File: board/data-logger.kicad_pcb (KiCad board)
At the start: 4 copper layers, 105 x 100 mm, 220 parts, among them P401 CONN_01X02, P402 CONN_01X04, P403 CONN_01X04, P501 CONN_02X03, P502 CONN_02X06, P503 MICROSD, P504 USB_B, P601 CONN_02X08, P602 CONN_02X08, P603 CONN_02X08, P604 CONN_02X08, Q401 IRLML6401, Q402 Q_NMOS_GSD, Q501 IRLML6401, U201 10M08DCF256, U202 AS4C8M16SA-7TCN, U203 AS4C8M16SA-7TCN, U302 SAM3U1EB-AU, U401 AP2138N-2.5TRG1, U402 LM4120, U403 BQ24161RGE, U404 TPS62097, U405 TPS62097, U406 AP2138N-2.5TRG1, U407 TPS63001, U501 LSF0204, U502 LSF0204, U601 MCP6002, X501 CONN_DEBUG_MCNET, X502 IQXO/7X, Y501 32.768 kHz, Y502 12.000MHz

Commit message: Save last pcb layout work
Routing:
- net Net-(C441-Pad1): track 0.71 -> 5.52 mm, vias 1 -> 2
- net /InterConnect/FPGA_CRC_ERROR: track 4.54 -> 8.15 mm, vias 0 -> 1
- net /InterConnect/SMC_D3: track 0.00 -> 3.61 mm, vias 0 -> 1
- net /InterConnect/SMC_D2: track 0.00 -> 3.61 mm, vias 0 -> 1
- net /InterConnect/SMC_D10: track 0.00 -> 3.56 mm, vias 0 -> 1
- net /InterConnect/SMC_NWAIT: track 0.00 -> 2.61 mm
- net /InterConnect/SMC_D11: track 0.00 -> 2.61 mm
- net /InterConnect/SMC_A14: track 0.00 -> 2.61 mm
- net /InterConnect/SMC_A12: track 0.00 -> 2.61 mm
- net /InterConnect/SMC_A17: track 0.00 -> 1.40 mm
- net /InterConnect/SMC_A16: track 0.00 -> 1.40 mm
- net /InterConnect/SMC_A15: track 0.00 -> 1.40 mm
- net /InterConnect/SMC_A13: track 0.00 -> 1.35 mm
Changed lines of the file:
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@@
   (general
     (links 900)
-    (no_connects 480)
-    (area 17.424999 33.424999 122.575001 133.575001)
+    (no_connects 464)
+    (area 13.174999 10.775 129.295001 149.100001)
     (thickness 1.6)
     (drawings 12)
-    (tracks 1926)
+    (tracks 1955)
     (zones 0)
     (modules 220)
@@
   )
   (setup
-    (last_trace_width 0.2)
+    (last_trace_width 0.15)
     (user_trace_width 0.15)
     (user_trace_width 0.2)
@@
   (segment (start 41.135998 108.5) (end 42.035998 107.6) (width 0.2) (layer F.Cu) (net 137))
   (segment (start 42.035998 107.6) (end 42.95 107.6) (width 0.2) (layer F.Cu) (net 137))
+  (segment (start 71.35 84.5) (end 68.45 84.5) (width 0.15) (layer B.Cu) (net 138))
+  (segment (start 71.85 84) (end 71.35 84.5) (width 0.15) (layer F.Cu) (net 138))
+  (via (at 71.35 84.5) (size 0.5) (drill 0.2) (layers F.Cu B.Cu) (net 138))
   (segment (start 42.95 105.6) (end 41.975 105.6) (width 0.2) (layer F.Cu) (net 138))
   (segment (start 41.975 105.6) (end 40.675 106.9) (width 0.2) (layer F.Cu) (net 138))
@@
   (segment (start 89.1 107.1) (end 89.1 106.225) (width 0.15) (layer F.Cu) (net 163))
   (segment (start 89.1 106.225) (end 88.475 105.6) (width 0.15) (layer F.Cu) (net 163))
+  (segment (start 69.85 87) (end 68.45 87) (width 0.15) (layer F.Cu) (net 166))
+  (segment (start 70.35 87.5) (end 68.45 87.5) (width 0.15) (layer F.Cu) (net 167))
+  (segment (start 70.85 87) (end 70.35 87.5) (width 0.15) (layer F.Cu) (net 167))
+  (segment (start 71.35 87.5) (end 68.5 87.5) (width 0.15) (layer B.Cu) (net 168))
+  (segment (start 71.85 87) (end 71.35 87.5) (width 0.15) (layer F.Cu) (net 168))
+  (via (at 71.35 87.5) (size 0.5) (drill 0.2) (layers F.Cu B.Cu) (net 168))
   (segment (start 42.95 110.6) (end 40.9 110.6) (width 0.2) (layer F.Cu) (net 172))
+  (segment (start 69.85 86) (end 68.45 86) (width 0.15) (layer F.Cu) (net 173))
+  (segment (start 70.35 86.5) (end 68.45 86.5) (width 0.15) (layer F.Cu) (net 174))
+  (segment (start 70.600001 86.249999) (end 70.35 86.5) (width 0.15) (layer F.Cu) (net 174))
+  (segment (start 70.85 86) (end 70.600001 86.249999) (width 0.15) (layer F.Cu) (net 174))
+  (segment (start 71.35 86.5) (end 68.45 86.5) (width 0.15) (layer B.Cu) (net 175))
+  (segment (start 71.85 86) (end 71.35 86.5) (width 0.15) (layer F.Cu) (net 175))
+  (via (at 71.35 86.5) (size 0.5) (drill 0.2) (layers F.Cu B.Cu) (net 175))
+  (segment (start 69.85 85) (end 68.45 85) (width 0.15) (layer F.Cu) (net 180))
+  (segment (start 70.35 85.5) (end 68.45 85.5) (width 0.15) (layer F.Cu) (net 181))
+  (segment (start 70.85 85) (end 70.35 85.5) (width 0.15) (layer F.Cu) (net 181))
+  (segment (start 71.35 85.5) (end 68.45 85.5) (width 0.15) (layer B.Cu) (net 182))
+  (via (at 71.35 85.5) (size 0.5) (drill 0.2) (layers F.Cu B.Cu) (net 182))
+  (segment (start 71.85 85) (end 71.35 85.5) (width 0.15) (layer F.Cu) (net 182))
+  (segment (start 69.85 84) (end 68.5 84) (width 0.15) (layer F.Cu) (net 186))
+  (segment (start 70.35 84.5) (end 68.45 84.5) (width 0.15) (layer F.Cu) (net 187))
+  (segment (start 70.85 84) (end 70.35 84.5) (width 0.15) (layer F.Cu) (net 187))
   (segment (start 71.385 36.6) (end 80.95 36.6) (width 0.3) (layer F.Cu) (net 212))
   (segment (start 92.25 36.6) (end 95.285 36.6) (width 0.3) (layer F.Cu) (net 212))
@@
   (segment (start 33.235 45.2) (end 32.15 45.2) (width 0.3) (layer F.Cu) (net 263))
   (segment (start 32.15 45.2) (end 31.7 44.75) (width 0.3) (layer F.Cu) (net 263))
+  (segment (start 71.85 85) (end 68.45 85) (width 0.15) (layer B.Cu) (net 265))
+  (segment (start 72.35 84.5) (end 71.85 85) (width 0.15) (layer B.Cu) (net 265))
+  (segment (start 72.85 84) (end 72.35 84.5) (width 0.15) (layer F.Cu) (net 265))
+  (via (at 72.35 84.5) (size 0.5) (drill 0.2) (layers F.Cu B.Cu) (net 265))
   (via (at 80.35 77.5) (size 0.5) (drill 0.2) (layers F.Cu B.Cu) (net 265))
   (segment (start 80.85 77) (end 80.35 77.5) (width 0.3) (layer F.Cu) (net 265))

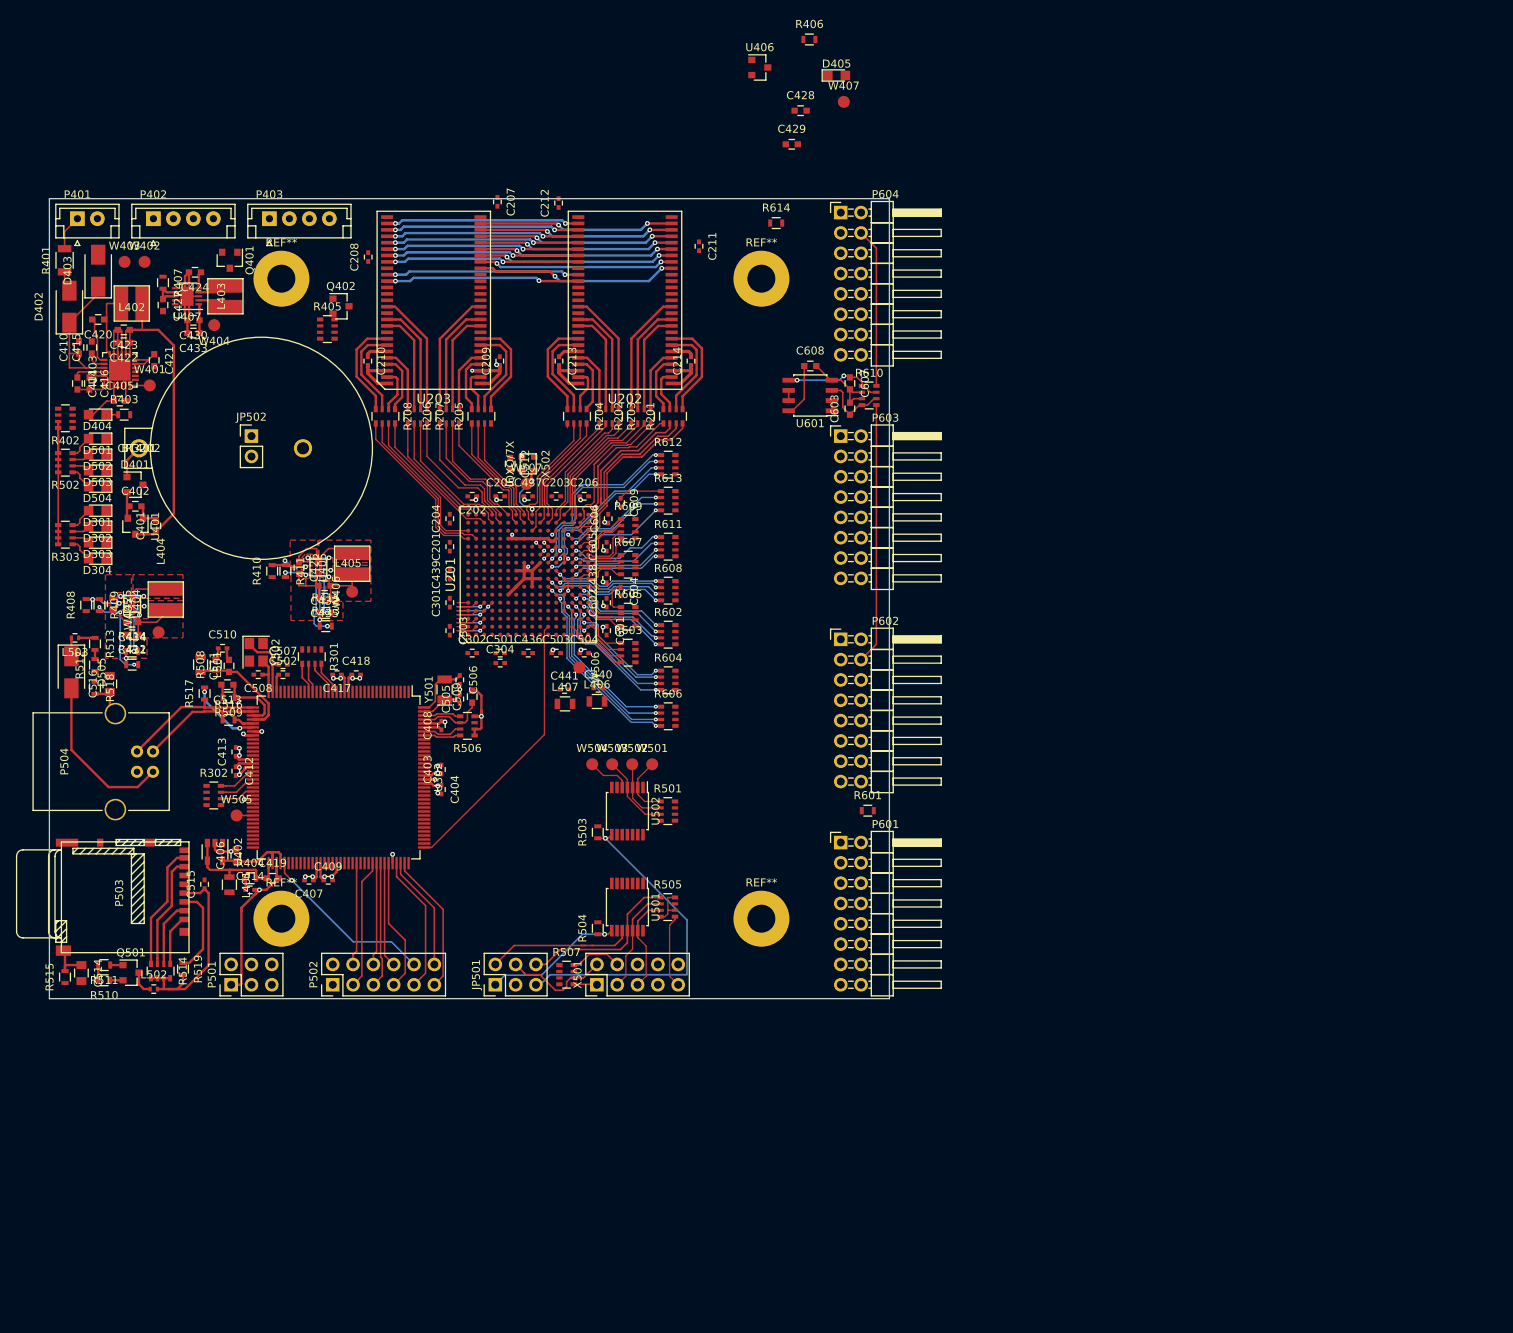
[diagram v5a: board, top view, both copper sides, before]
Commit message: Some initial DDR3 Ram routing
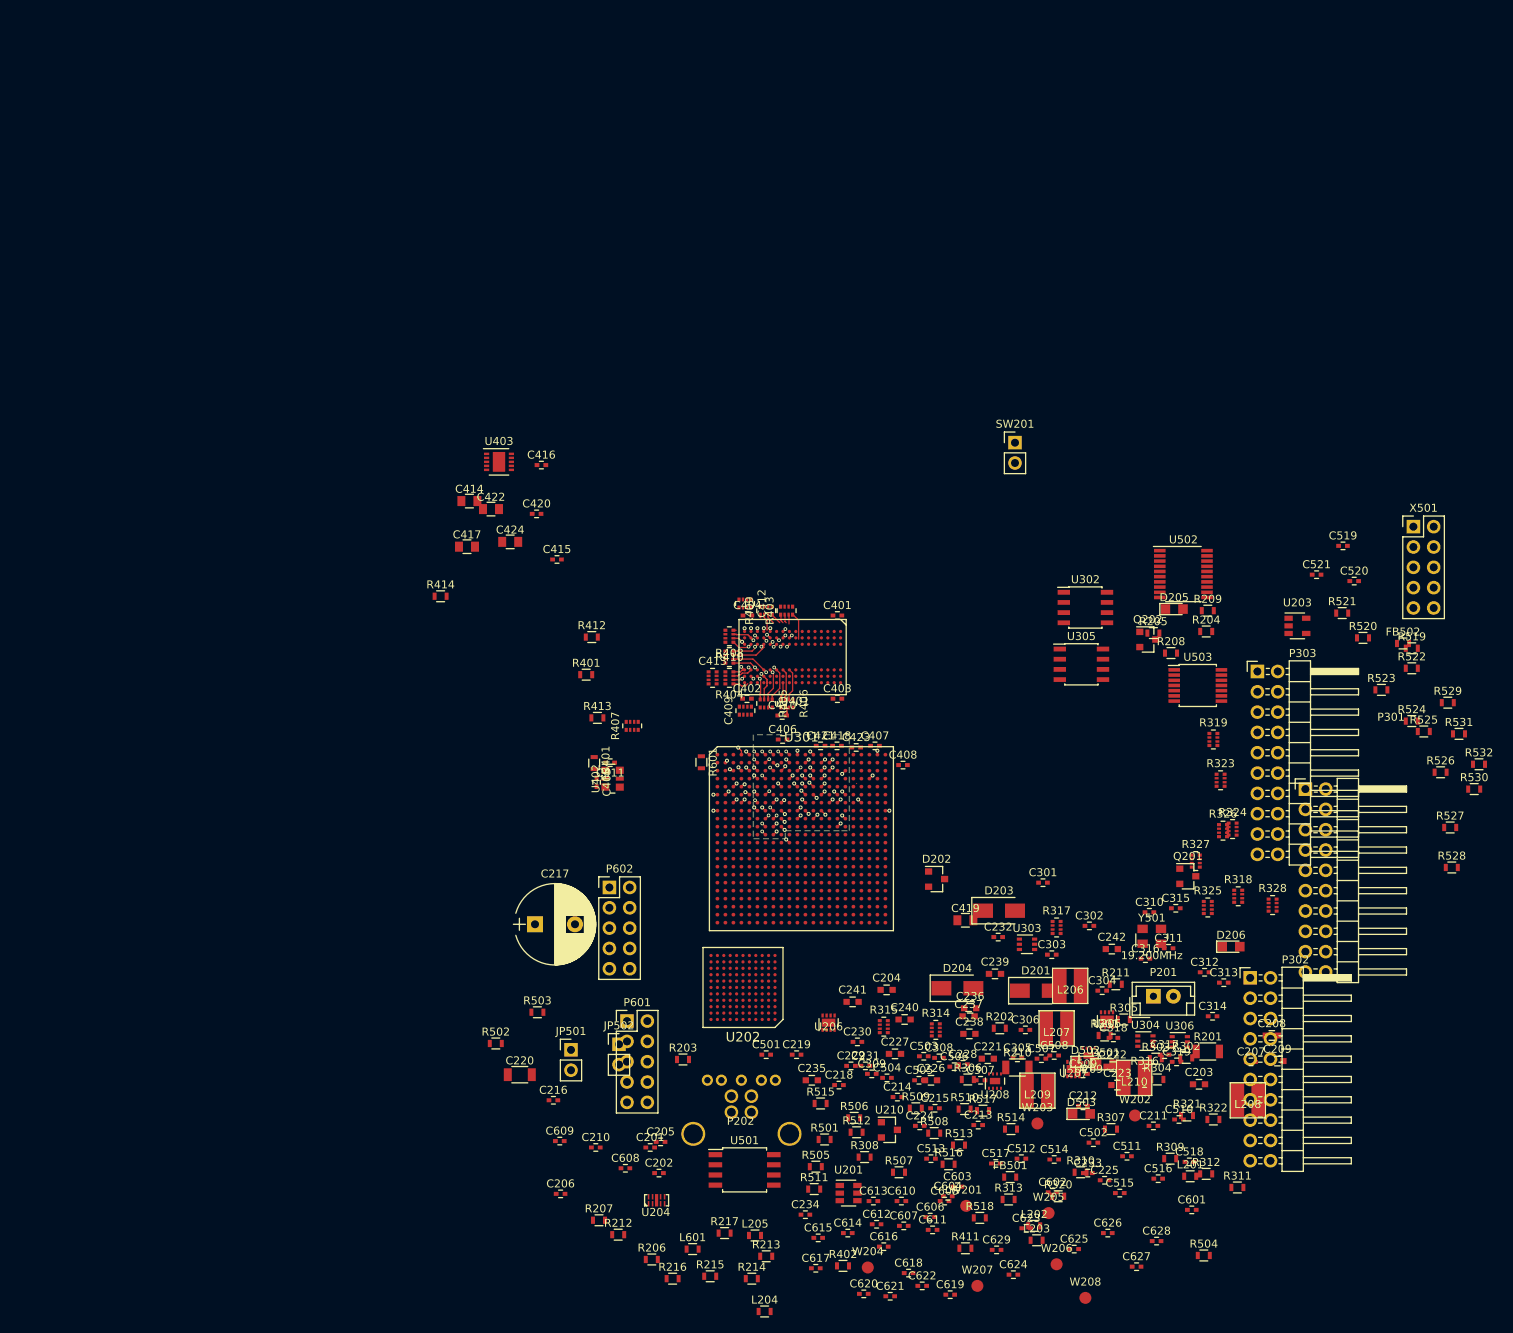
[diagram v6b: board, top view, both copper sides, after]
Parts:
- removed BT401: CR3202, AMesser_Connectors:keystone_electronics_106
- removed C425, C426, C430, C431, C432, C433, C434, C435: 10µF, Capacitors_SMD:C_0603
- removed C427: 10nF, Capacitors_SMD:C_0603
- removed C428, C429: 1µF, Capacitors_SMD:C_0603
- removed C436, C437, C438, C439, C440, C441: 4.7µF, Capacitors_SMD:C_0402
- removed D301, D302, D303, D304, D404, D405, D504: Led_Small, LEDs:LED_0805
- removed D401: BAT54C, TO_SOT_Packages_SMD:SOT-23
- removed D402: D_Schottky, Diodes_SMD:D_SMA_Standard
- removed D403: ZENER, Diodes_SMD:D_SMA_Standard
- removed D505: SS12, Diodes_SMD:D_SMA_Standard
- removed L401, L406, L407, L501: 4.7µH, Resistors_SMD:R_0805
- removed L402, L403: 2.2µH, AMesser_Inductors:Bourns_SRN4018TA
- removed L404, L405: 1µH, AMesser_Inductors:Bourns_SRN4018TA
- removed L502, L503: 470nH, Resistors_SMD:R_0402
- removed P401: CONN_01X02, Connectors_JST:JST_EH_B02B-EH-A_02x2.50mm_Straight
- removed P402, P403: CONN_01X04, Connectors_JST:JST_EH_B04B-EH-A_04x2.50mm_Straight
- removed P501: CONN_02X03, Pin_Headers:Pin_Header_Straight_2x03_Pitch2.54mm
- removed P502: CONN_02X06, Pin_Headers:Pin_Header_Straight_2x06_Pitch2.54mm
- removed P503: MICROSD, AMesser_Connectors:Hirose_DM3AT
- removed P504: USB_B, Connect:USB_B
- removed P603, P604: CONN_02X08, Pin_Headers:Pin_Header_Angled_2x08_Pitch2.54mm
- removed Q401, Q501: IRLML6401, TO_SOT_Packages_SMD:SOT-23
- removed Q402: Q_NMOS_GSD, TO_SOT_Packages_SMD:SOT-23
- removed R415: 10.0k, Resistors_SMD:R_0603
- removed R602, R603, R604, R605, R606, R607, R608, R609, R611, R612, R613: 22, Resistors_SMD:R_Array_Convex_4x0603
- removed R610: 10k, Resistors_SMD:R_Array_Convex_4x0603
- removed R614: 6.8k, Resistors_SMD:R_0603
- removed REF** (x4): MountingHole_3.5mm_Pad, Mounting_Holes:MountingHole_3.5mm_Pad
- removed U404, U405: TPS62097, AMesser_Power_Management:Texas_Instruments_VQFN-HR-11
- removed U406: AP2138N-2.5TRG1, TO_SOT_Packages_SMD:SOT-23
- removed U407: TPS63001, AMesser_Power_Management:Texas_Instruments_PVSON-N10
- removed U601: MCP6002, Housings_SOIC:SOIC-8_3.9x4.9mm_Pitch1.27mm
- removed W401, W402, W403, W404, W405, W406, W407, W501, W502, W503, W504, W505, W506, W507: TEST_1P, Measurement_Points:Measurement_Point_Round-SMD-Pad_Small
- removed X502: IQXO/7X, amesser-special:ASDMB
- removed Y502: 12.000MHz, Crystals:Crystal_SMD_Abracon_ABM8G-4pin_3.2x2.5mm
- added C215: 100n, Capacitors_SMD:C_0402, F.Cu at (128.2, 147.2)
- added C216: 100nF, Capacitors_SMD:C_0402, F.Cu at (80.5, 146.2)
- added C217: 470µF, Capacitors_ThroughHole:CP_Radial_D10.0mm_P5.00mm, F.Cu at (78.2, 124.2)
- added C218: 100n, Capacitors_SMD:C_0402, F.Cu at (116.2, 144.3)
- added C219: 100n, Capacitors_SMD:C_0402, F.Cu at (110.9, 140.5)
- added C220: 100n, Capacitors_SMD:C_1206, F.Cu at (76.3, 143.0)
- added C221: 10µF, Capacitors_SMD:C_0603, F.Cu at (134.8, 141.0)
- added C222: 10µF, Capacitors_SMD:C_0603, F.Cu at (150.4, 142.0)
- added C223: 10µF, Capacitors_SMD:C_0603, F.Cu at (151.0, 144.3)
- added C224: 4.7µF, Capacitors_SMD:C_0402, F.Cu at (126.3, 149.4)
- added C225: 4.7µF, Capacitors_SMD:C_0402, F.Cu at (149.4, 156.2)
- added C226: 1µF, Capacitors_SMD:C_0603, F.Cu at (127.7, 143.7)
- added C227: 1µF, Capacitors_SMD:C_0603, F.Cu at (123.2, 140.4)
- added C228: 560p, Capacitors_SMD:C_0402, F.Cu at (131.7, 141.7)
- added C229: 560p, Capacitors_SMD:C_0402, F.Cu at (117.7, 141.9)
- added C230: 15pF, Capacitors_SMD:C_0402, F.Cu at (118.5, 138.9)
- added C231: 27p, Capacitors_SMD:C_0402, F.Cu at (119.5, 141.9)
- added C232: 27pF, Capacitors_SMD:C_0402, F.Cu at (136.1, 125.8)
- added C233: 4.7µF, Capacitors_SMD:C_0402, F.Cu at (147.3, 155.3)
- added C234: 4.7µF, Capacitors_SMD:C_0402, F.Cu at (112.0, 160.5)
- added C235: 10µF, Capacitors_SMD:C_0603, F.Cu at (112.8, 143.7)
- added C236: 10µF, Capacitors_SMD:C_0603, F.Cu at (132.6, 134.7)
- added C237: 10µF, Capacitors_SMD:C_0603, F.Cu at (132.4, 135.7)
- added C238: 10µF, Capacitors_SMD:C_0603, F.Cu at (132.5, 137.9)
- added C239: 10µF, Capacitors_SMD:C_0603, F.Cu at (135.7, 130.4)
- added C240: 10µF, Capacitors_SMD:C_0603, F.Cu at (124.4, 136.1)
- added C241: 10µF, Capacitors_SMD:C_0603, F.Cu at (117.9, 133.9)
- added C242: 10µF, Capacitors_SMD:C_0603, F.Cu at (150.3, 127.3)
- added C305: 100n, Capacitors_SMD:C_0402, F.Cu at (138.5, 140.9)
- added C306: 100n, Capacitors_SMD:C_0402, F.Cu at (139.5, 137.4)
- added C307: 100n, Capacitors_SMD:C_0402, F.Cu at (133.9, 143.7)
- added C308: 100n, Capacitors_SMD:C_0402, F.Cu at (128.7, 140.9)
- added C309: 100n, Capacitors_SMD:C_0402, F.Cu at (120.3, 142.9)
- added C310: 4µ7, Capacitors_SMD:C_0402, F.Cu at (155.0, 122.7)
- added C311: 4µ7, Capacitors_SMD:C_0402, F.Cu at (157.4, 127.2)
- added C312: 4µ7, Capacitors_SMD:C_0402, F.Cu at (161.9, 130.2)
- added C313: 4µ7, Capacitors_SMD:C_0402, F.Cu at (164.3, 131.5)
- added C314: 1n, Capacitors_SMD:C_0402, F.Cu at (162.9, 135.7)
- added C315: 1n, Capacitors_SMD:C_0402, F.Cu at (158.3, 122.2)
- added C316: 100n, Capacitors_SMD:C_0402, F.Cu at (154.5, 128.5)
- added C317: 100n, Capacitors_SMD:C_0402, F.Cu at (156.9, 140.5)
- added C318: 1n, Capacitors_SMD:C_0402, F.Cu at (150.5, 138.4)
- added C319: 100n, Capacitors_SMD:C_0402, F.Cu at (158.4, 141.4)
- added C517: 100n, Capacitors_SMD:C_0402, F.Cu at (135.8, 154.1)
- added C518: 10p, Capacitors_SMD:C_0402, F.Cu at (160.0, 153.9)
- added C519: 100n, Capacitors_SMD:C_0402, F.Cu at (179.2, 76.9)
- added C520: 4µ7, Capacitors_SMD:C_0402, F.Cu at (180.6, 81.3)
- added C521: 100n, Capacitors_SMD:C_0402, F.Cu at (175.9, 80.5)
- added C610: 4µ7, Capacitors_SMD:C_0402, F.Cu at (124.0, 158.8)
- added C611: 4µ7, Capacitors_SMD:C_0402, F.Cu at (127.9, 162.4)
- added C612: 4µ7, Capacitors_SMD:C_0402, F.Cu at (120.9, 161.7)
- added C613: 4µ7, Capacitors_SMD:C_0402, F.Cu at (120.5, 158.8)
- added C614: 4µ7, Capacitors_SMD:C_0402, F.Cu at (117.3, 162.8)
- added C615: 4µ7, Capacitors_SMD:C_0402, F.Cu at (113.6, 163.4)
- added C616: 4µ7, Capacitors_SMD:C_0402, F.Cu at (121.8, 164.5)
- added C617: 4µ7, Capacitors_SMD:C_0402, F.Cu at (113.3, 167.2)
- added C618: 4µ7, Capacitors_SMD:C_0402, F.Cu at (124.9, 167.8)
- added C619: 4µ7, Capacitors_SMD:C_0402, F.Cu at (130.1, 170.5)
- added C620: 4µ7, Capacitors_SMD:C_0402, F.Cu at (119.3, 170.4)
- added C621: 4µ7, Capacitors_SMD:C_0402, F.Cu at (122.6, 170.7)
- added C622: 4µ7, Capacitors_SMD:C_0402, F.Cu at (126.6, 169.4)
- added C623: 100n, Capacitors_SMD:C_0402, F.Cu at (139.6, 162.2)
- added C624: 4µ7, Capacitors_SMD:C_0402, F.Cu at (138.0, 168.0)
- added C625: 4µ7, Capacitors_SMD:C_0402, F.Cu at (145.6, 164.8)
- added C626: 4µ7, Capacitors_SMD:C_0402, F.Cu at (149.8, 162.8)
- added C627: 100n, Capacitors_SMD:C_0402, F.Cu at (153.4, 167.0)
- added C628: 4µ7, Capacitors_SMD:C_0402, F.Cu at (155.9, 163.8)
- added C629: 4µ7, Capacitors_SMD:C_0402, F.Cu at (135.9, 164.9)
- added D201: D_TVS, Diodes_SMD:D_SMA, F.Cu at (140.8, 132.5)
- added D202: D, Diodes_SMD:D_SOT-23_ANK, F.Cu at (128.4, 118.5)
- added D203: D_Schottky, Diodes_SMD:D_SMA, F.Cu at (136.2, 122.5)
- added D204: D_TVS, Diodes_SMD:D_SMA, F.Cu at (131.0, 132.2)
- added D205: Led_Small, LEDs:LED_0805, F.Cu at (158.1, 84.8)
- added D206: LED_Small, LEDs:LED_0805, F.Cu at (165.2, 127.0)
- added FB401: BLM18KG, Resistors_SMD:R_0603, F.Cu at (85.6, 104.0)
- added FB501: BLM18KG, Resistors_SMD:R_0603, F.Cu at (137.6, 155.8)
- added FB502: BLM18KG, Resistors_SMD:R_0603, F.Cu at (186.7, 89.1)
- added L201: BLM18KG, Resistors_SMD:R_0603, F.Cu at (160.1, 155.7)
- added L202: BLM18KG, Resistors_SMD:R_0603, F.Cu at (140.6, 161.9)
- added L203: BLM18KG, Resistors_SMD:R_0603, F.Cu at (140.9, 163.7)
- added L204: BLM18KG, Resistors_SMD:R_0603, F.Cu at (106.9, 172.6)
- added L205: BLM18KG, Resistors_SMD:R_0603, F.Cu at (105.7, 163.1)
- added L206: 1µH, AMesser_Inductors:Bourns_SRN4018TA, F.Cu at (145.1, 131.9)
- added L207: 2.2µH, AMesser_Inductors:Bourns_SRN4018TA, F.Cu at (143.4, 137.2)
- added L208: 2.2µH, AMesser_Inductors:Bourns_SRN4018TA, F.Cu at (167.3, 146.2)
- added L209: 2.2µH, AMesser_Inductors:Bourns_SRN4018TA, F.Cu at (141.0, 145.0)
- added L210: 2.2µH, AMesser_Inductors:Bourns_SRN4018TA, F.Cu at (153.1, 143.4)
- added L601: BLM18KG, Resistors_SMD:R_0603, F.Cu at (97.9, 164.8)
- added P201: CONN_01X02, Connectors_JST:JST_EH_B02B-EH-A_02x2.50mm_Straight, F.Cu at (155.5, 133.2)
- added P202: USB_B_3, AMesser_Connectors:Amphenol_GSB3211XXXWEU, F.Cu at (104.0, 150.4)
- added P301: CONN_02X10, Pin_Headers:Pin_Header_Angled_2x10_Pitch2.54mm, F.Cu at (174.5, 107.3)
- added P302: CONN_02X10, Pin_Headers:Pin_Header_Angled_2x10_Pitch2.54mm, F.Cu at (167.6, 130.9)
- added P303: CONN_02X10, Pin_Headers:Pin_Header_Angled_2x10_Pitch2.54mm, F.Cu at (168.5, 92.6)
- added Q201: IRLML6344TRPBF, TO_SOT_Packages_SMD:SOT-23, F.Cu at (159.8, 118.2)
- added Q202: Q_NPN_BEC, TO_SOT_Packages_SMD:SOT-23, F.Cu at (154.8, 88.6)
- added R209: 470, Resistors_SMD:R_0603, F.Cu at (162.3, 85.0)
- added R210: 1M, Resistors_SMD:R_1206, F.Cu at (138.5, 142.1)
- added R211: 100k, Resistors_SMD:R_0603, F.Cu at (150.8, 131.7)
- added R212: 220k 1%, Resistors_SMD:R_0603, F.Cu at (88.6, 163.0)
- added R213: 261k 1%, Resistors_SMD:R_0603, F.Cu at (107.1, 165.7)
- added R214: 220k 1%, Resistors_SMD:R_0603, F.Cu at (105.3, 168.5)
- added R215: 178k 1%, Resistors_SMD:R_0603, F.Cu at (100.1, 168.2)
- added R216: 220k 1%, Resistors_SMD:R_0603, F.Cu at (95.4, 168.5)
- added R217: 69.8k 1%, Resistors_SMD:R_0603, F.Cu at (101.9, 162.8)
- added R304: 470R, Resistors_SMD:R_0603, F.Cu at (156.0, 143.6)
- added R305: 470R, Resistors_SMD:R_0603, F.Cu at (151.8, 136.1)
- added R306: 470R, Resistors_SMD:R_0603, F.Cu at (132.3, 143.6)
- added R307: 100R, Resistors_SMD:R_0603, F.Cu at (150.2, 149.8)
- added R308: 4k7, Resistors_SMD:R_0603, F.Cu at (119.4, 153.3)
- added R309: 4k7, Resistors_SMD:R_0603, F.Cu at (157.6, 153.5)
- added R310: 4k7, Resistors_SMD:R_0603, F.Cu at (146.4, 155.2)
- added R311: 4k7, Resistors_SMD:R_0603, F.Cu at (166.0, 157.1)
- added R312: 100k, Resistors_SMD:R_0603, F.Cu at (162.1, 155.4)
- added R313: 100k, Resistors_SMD:R_0603, F.Cu at (137.4, 158.6)
- added R314: 51R, Resistors_SMD:R_Array_Convex_4x0402, F.Cu at (128.3, 137.4)
- added R315: 51R, Resistors_SMD:R_Array_Convex_4x0402, F.Cu at (121.8, 137.0)
- added R316: 51R, Resistors_SMD:R_Array_Convex_4x0402, F.Cu at (154.4, 143.4)
- added R317: 51R, Resistors_SMD:R_Array_Convex_4x0402, F.Cu at (143.4, 124.6)
- added R318: 51R, Resistors_SMD:R_Array_Convex_4x0402, F.Cu at (166.1, 120.7)
- added R319: 51R, Resistors_SMD:R_Array_Convex_4x0402, F.Cu at (163.0, 101.1)
- added R320: 4k7, Resistors_SMD:R_0603, F.Cu at (143.6, 158.2)
- added R321: 4k7, Resistors_SMD:R_0603, F.Cu at (159.7, 148.1)
- added R322: 100k, Resistors_SMD:R_0603, F.Cu at (163.0, 148.6)
- added R323: 51R, Resistors_SMD:R_Array_Convex_4x0402, F.Cu at (163.9, 106.2)
- added R324: 51R, Resistors_SMD:R_Array_Convex_4x0402, F.Cu at (165.4, 112.3)
- added R325: 51R, Resistors_SMD:R_Array_Convex_4x0402, F.Cu at (162.3, 122.1)
- added R326: 51R, Resistors_SMD:R_Array_Convex_4x0402, F.Cu at (164.2, 112.5)
- added R327: 51R, Resistors_SMD:R_Array_Convex_4x0402, F.Cu at (160.8, 116.3)
- added R328: 51R, Resistors_SMD:R_Array_Convex_4x0402, F.Cu at (170.4, 121.8)
- added R520: 10k, Resistors_SMD:R_0603, F.Cu at (181.7, 88.4)
- added R521: 10k, Resistors_SMD:R_0603, F.Cu at (179.1, 85.3)
- added R522: 10k, Resistors_SMD:R_0603, F.Cu at (187.8, 92.2)
- added R523: 1k, Resistors_SMD:R_0603, F.Cu at (184.0, 94.9)
- added R524: 10k, Resistors_SMD:R_0603, F.Cu at (187.8, 98.8)
- added R525: 100R, Resistors_SMD:R_0603, F.Cu at (189.3, 100.1)
- added R526: 4k7, Resistors_SMD:R_0603, F.Cu at (191.4, 105.2)
- added R527: 4k7, Resistors_SMD:R_0603, F.Cu at (192.6, 112.1)
- added R528: 4k7, Resistors_SMD:R_0603, F.Cu at (192.8, 117.1)
- added R529: 200k, Resistors_SMD:R_0603, F.Cu at (192.3, 96.5)
- added R530: 1k8, Resistors_SMD:R_0603, F.Cu at (195.6, 107.3)
- added R531: 1k8, Resistors_SMD:R_0603, F.Cu at (193.7, 100.4)
- added R532: 1k8, Resistors_SMD:R_0603, F.Cu at (196.2, 104.2)
- added SW201: SW_Push, Pin_Headers:Pin_Header_Straight_1x02_Pitch2.54mm, F.Cu at (138.2, 64.0)
- added U204: SP3010-04UTG, AMesser_Misc:SP3010, F.Cu at (93.4, 158.7)
- added U205: NCP6324B, AMesser_Power_Management:ON_Semiconductor_WDFN-8_2x2mm_Pitch0.5mm, F.Cu at (149.7, 136.1)
- added U206: NCP6332B, AMesser_Power_Management:ON_Semiconductor_WDFN-8_2x2mm_Pitch0.5mm, F.Cu at (114.9, 136.5)
- added U207: NCP6332B, AMesser_Power_Management:ON_Semiconductor_WDFN-8_2x2mm_Pitch0.5mm, F.Cu at (145.5, 142.3)
- added U208: MIC23050-4YML, AMesser_Power_Management:Micrel_MLF-8_2x2mm_Pitch0.5mm, F.Cu at (135.7, 143.8)
- added U209: MIC23050-SYML, AMesser_Power_Management:Micrel_MLF-8_2x2mm_Pitch0.5mm, F.Cu at (147.4, 140.6)
- added U210: AP2138N-1.8TRG1, TO_SOT_Packages_SMD:SOT-23, F.Cu at (122.5, 149.9)
- added U301: 5CEFA2F23, board_footprints:BGA_484_Pitch1.0, F.Cu at (111.5, 113.5)
- added U303: FSA5157P6X, TO_SOT_Packages_SMD:SOT-363_SC-70-6, F.Cu at (139.7, 126.7)
- added U304: FSA5157P6X, TO_SOT_Packages_SMD:SOT-363_SC-70-6, F.Cu at (154.5, 138.8)
- added U305: LMC6062, Housings_SOIC:SOIC-8_3.9x4.9mm_Pitch1.27mm, F.Cu at (146.5, 91.7)
- added U306: FSA5157P6X, TO_SOT_Packages_SMD:SOT-363_SC-70-6, F.Cu at (158.8, 138.9)
- added U503: CDCE913, Housings_SSOP:TSSOP-14_4.4x5mm_Pitch0.65mm, F.Cu at (161.1, 94.3)
- added W201: TEST_1P, Measurement_Points:Measurement_Point_Round-SMD-Pad_Small, F.Cu at (132.1, 159.4)
- added W202: TEST_1P, Measurement_Points:Measurement_Point_Round-SMD-Pad_Small, F.Cu at (153.2, 148.1)
- added W203: TEST_1P, Measurement_Points:Measurement_Point_Round-SMD-Pad_Small, F.Cu at (141.0, 149.1)
- added W204: TEST_1P, Measurement_Points:Measurement_Point_Round-SMD-Pad_Small, F.Cu at (119.8, 167.1)
- added W205: TEST_1P, Measurement_Points:Measurement_Point_Round-SMD-Pad_Small, F.Cu at (142.4, 160.3)
- added W206: TEST_1P, Measurement_Points:Measurement_Point_Round-SMD-Pad_Small, F.Cu at (143.4, 166.7)
- added W207: TEST_1P, Measurement_Points:Measurement_Point_Round-SMD-Pad_Small, F.Cu at (133.5, 169.4)
- added W208: TEST_1P, Measurement_Points:Measurement_Point_Round-SMD-Pad_Small, F.Cu at (147.0, 170.9)
- C203, C204, C208, C209: value 4.7µF -> 10µF; footprint Capacitors_SMD:C_0402 -> Capacitors_SMD:C_0603
- C207, C211, C212, C213, C214, C304: value 4.7µF -> 100n
- C301, C302, C303, C403, C404, C407, C408, C418, C501, C503, C504, C510, C601, C602, C604, C605, C606, C609: value 4.7µF -> 4µ7
- C401, C402: value 1µF -> 4µ7; footprint Capacitors_SMD:C_0603 -> Capacitors_SMD:C_0402
- C405, C410: value 1µF -> 100n; footprint Capacitors_SMD:C_0603 -> Capacitors_SMD:C_0402
- C406: value 22n -> 4µ7; footprint Capacitors_SMD:C_0603 -> Capacitors_SMD:C_0402
- C409, C412, C413: value 4.7µF -> 100nF; footprint Capacitors_SMD:C_0402 -> Resistors_SMD:R_Array_Convex_4x0402
- C411: value 1µF -> 100n n.p.; footprint Capacitors_SMD:C_0603 -> Capacitors_SMD:C_0402
- C414, C417: value 4.7µF -> 10µ; footprint Capacitors_SMD:C_0402 -> Capacitors_SMD:C_0805
- C415: value 4.7µF -> 100n; footprint Capacitors_SMD:C_0603 -> Capacitors_SMD:C_0402
- C416: value 4.7µF -> 4µ7; footprint Capacitors_SMD:C_0603 -> Capacitors_SMD:C_0402
- C419: value 100nF -> 10µ; footprint Capacitors_SMD:C_0603 -> Capacitors_SMD:C_0805
- C420: value 10nF -> 100n; footprint Capacitors_SMD:C_0603 -> Capacitors_SMD:C_0402
- C421, C423: value 10µF -> 4µ7; footprint Capacitors_SMD:C_0603 -> Capacitors_SMD:C_0402
- C422, C424: value 10µF -> 10µ; footprint Capacitors_SMD:C_0603 -> Capacitors_SMD:C_0805
- C502: value 100nF -> 4µ7
- C505, C506, C508: value 20pF -> 4µ7
- C507: value 20pF -> 100n
- C509: value 10nF -> 4µ7; footprint Capacitors_SMD:C_0603 -> Capacitors_SMD:C_0402
- C511, C512, C603, C607, C608: value 100nF -> 4µ7; footprint Capacitors_SMD:C_0603 -> Capacitors_SMD:C_0402
- C513: value 10pF -> 4µ7; footprint Capacitors_SMD:C_0603 -> Capacitors_SMD:C_0402
- C514, C516: value 100nF -> 4µ7; footprint Capacitors_SMD:C_0805 -> Capacitors_SMD:C_0402
- C515: value 4.7µF -> 10p
- D501, D502, D503: value Led_Small -> LED_Small
- JP501: value JUMPER_3X02 -> Jumper_NC_Small; footprint Pin_Headers:Pin_Header_Straight_2x03_Pitch2.54mm -> Pin_Headers:Pin_Header_Straight_1x02_Pitch2.54mm
- JP502: value Jumper_NO_Small -> Jumper_NC_Small
- P601, P602: value CONN_02X08 -> CONN_02X05; footprint Pin_Headers:Pin_Header_Angled_2x08_Pitch2.54mm -> Pin_Headers:Pin_Header_Straight_2x05_Pitch2.54mm
- R201: value 22 -> 0.01; footprint Resistors_SMD:R_Array_Convex_4x0603 -> Resistors_SMD:R_1206
- R202, R203: value 22 -> 4.7k; footprint Resistors_SMD:R_Array_Convex_4x0603 -> Resistors_SMD:R_0603
- R204: value 22 -> 100R; footprint Resistors_SMD:R_Array_Convex_4x0603 -> Resistors_SMD:R_0603
- R205: value 22 -> 1.5k; footprint Resistors_SMD:R_Array_Convex_4x0603 -> Resistors_SMD:R_0603
- R206: value 22 -> 6.04k / 1%; footprint Resistors_SMD:R_Array_Convex_4x0603 -> Resistors_SMD:R_0603
- R207: value 22 -> 200 / 1%; footprint Resistors_SMD:R_Array_Convex_4x0603 -> Resistors_SMD:R_0603
- R208: value 22 -> 10k; footprint Resistors_SMD:R_Array_Convex_4x0603 -> Resistors_SMD:R_0603
- R301, R302: value 10k -> 470R; footprint Resistors_SMD:R_Array_Convex_4x0603 -> Resistors_SMD:R_0603
- R303: value 330 -> 470R; footprint Resistors_SMD:R_Array_Convex_4x0603 -> Resistors_SMD:R_0603
- R401: value 0.01 -> 4k7; footprint Resistors_SMD:R_1206 -> Resistors_SMD:R_0603
- R402: value 10k -> 240; footprint Resistors_SMD:R_Array_Convex_4x0603 -> Resistors_SMD:R_0603
- R403, R408, R410: value 1.5k -> 51R; footprint Resistors_SMD:R_0603 -> Resistors_SMD:R_Array_Convex_4x0402
- R404: value 1 -> 51R; footprint Resistors_SMD:R_0603 -> Resistors_SMD:R_Array_Convex_4x0402
- R405: value 100k -> 51R; footprint Resistors_SMD:R_Array_Convex_4x0603 -> Resistors_SMD:R_Array_Convex_4x0402
- R406, R409: value 1.0k -> 51R; footprint Resistors_SMD:R_0603 -> Resistors_SMD:R_Array_Convex_4x0402
- R407: value 100 -> 51R; footprint Resistors_SMD:R_0603 -> Resistors_SMD:R_Array_Convex_4x0402
- R411: value 1.0k -> 10k
- R412, R413: value 20.0k -> 10k
- R414: value 24.9k -> 240
- R501, R505: footprint Resistors_SMD:R_Array_Convex_4x0603 -> Resistors_SMD:R_0603
- R502: value 330 -> 10k; footprint Resistors_SMD:R_Array_Convex_4x0603 -> Resistors_SMD:R_0603
- R503, R504, R510: value 22k -> 10k
- R506, R507: value 10k -> 470; footprint Resistors_SMD:R_Array_Convex_4x0603 -> Resistors_SMD:R_0603
- R508: value 1 -> 470
- R509: value 6.8k -> 10k
- R511: value 1.0k -> 0
- R512, R513: value 22k -> 0
- R514: value 68k -> 0; footprint Resistors_SMD:R_Array_Convex_4x0603 -> Resistors_SMD:R_0603
- R515: value 1M -> 0
- R516, R517: value 39.0 -> 10k
- R518: value 1M -> 10k
- R519: value 10k -> 1k8
- R601: value 6.8k -> 2.00k / 1%
- U201: value 10M08DCF256 -> LM5050-1; footprint board_footprints:FBGA_256 -> TO_SOT_Packages_SMD:SOT-23-6
- U202: value AS4C8M16SA-7TCN -> CYUSB3012-BZXC; footprint board_footprints:TSSOP-II-54 -> board_footprints:BGA_121_Pitch0.8
- U203: value AS4C8M16SA-7TCN -> R3111xxxB; footprint board_footprints:TSSOP-II-54 -> TO_SOT_Packages_SMD:SOT-23-5
- U302: value SAM3U1EB-AU -> LMC6062; footprint Housings_QFP:LQFP-144_20x20mm_Pitch0.5mm -> Housings_SOIC:SOIC-8_3.9x4.9mm_Pitch1.27mm
- U401: value AP2138N-2.5TRG1 -> IS43TR16256LA; footprint TO_SOT_Packages_SMD:SOT-23 -> AMesser_Misc:BGA-96_Pitch0.8mm
- U402: value LM4120 -> DSC1103CI5-100.0000; footprint TO_SOT_Packages_SMD:SOT-23-5 -> AMesser_Oscillators:Discera_DSC11xxC_3.2x2.5mm
- U403: value BQ24161RGE -> NCP51200; footprint board_footprints:VQFN-24_EP -> AMesser_Power_Management:DFN-10-1EP_3x3mm_Pitch0.5mm
- U501: value LSF0204 -> 25LC_EEPROM; footprint Housings_SSOP:TSSOP-14_4.4x5mm_Pitch0.65mm -> Housings_SOIC:SOIJ-8_5.3x5.3mm_Pitch1.27mm
- U502: value LSF0204 -> LSF0108; footprint Housings_SSOP:TSSOP-14_4.4x5mm_Pitch0.65mm -> Housings_SSOP:TSSOP-20_4.4x6.5mm_Pitch0.65mm
- Y501: value 32.768 kHz -> 19.200MHz; footprint Crystals:Crystal_SMD_EuroQuartz_EQ161-2pin_3.2x1.5mm -> AMesser_Oscillators:Crystal_SMD_3.2x2.5mm
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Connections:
- C201 pad 1: VCCIO_MCU -> VCC_1V20
- C202 pad 1: VCCIO_MCU -> VCC_1V20
- C203 pad 1: VCCIO_MCU -> Net-(C203-Pad1)
- C204 pad 1: VCCIO_MCU -> Net-(C204-Pad1)
- C205 pad 1: VCCIO_MCU -> VCC_1V20
- C206 pad 1: VCCIO_MCU -> Net-(C206-Pad1)
- C207 pad 1: VCCIO_MCU -> VCC_3V30
- C208 pad 1: VCCIO_MCU -> Net-(C203-Pad1)
- C209 pad 1: VCCIO_MCU -> Net-(C204-Pad1)
- C210 pad 1: VCCIO_MCU -> VCC_1V20
- C211 pad 1: VCCIO_MCU -> Net-(C211-Pad1)
- C212 pad 1: VCCIO_MCU -> Net-(C206-Pad1)
- C213 pad 1: VCCIO_MCU -> /FX3 USB & Power Supply/VCC_USB
- C214 pad 1: VCCIO_MCU -> Net-(C203-Pad1)
- C301 pad 1: VCCIO_MCU -> /Cyclone V User IO/VCCIO_IO_A
- C302 pad 1: VCCIO_MCU -> /Cyclone V User IO/VCCIO_IO_A
- C303 pad 1: VCCIO_MCU -> /Cyclone V User IO/VCCIO_IO_A
- C304 pad 1: VCCIO_MCU -> /Cyclone V User IO/VCCIO_IO_A
- C304 pad 2: GND -> /Cyclone V User IO/VREF_B4
- C401 pad 1: /Power Supply/VCC_SYS -> VCC_1V35
- C402 pad 1: Net-(C402-Pad1) -> VCC_1V35
- C403 pad 1: VCCIO_MCU -> VCC_1V35
- C404 pad 1: +1V8 -> VCC_1V35
- C406 pad 1: /Power Supply/VREF_2V5 -> VCC_1V35
- C407 pad 1: VCCIO_MCU -> VCC_1V35
- C408 pad 1: VCCBU_MCU -> VCC_1V35
- C409 pad 1: +1V8 -> GND
- C410 pad 1: Net-(C410-Pad1) -> /Cyclone V DDR3 RAM/VTT_DDR3
- C410 pad 2: GND -> Net-(C410-Pad2)
- C411 pad 1: VCC_USB -> /Cyclone V DDR3 RAM/VTT_DDR3
- C411 pad 2: GND -> Net-(C411-Pad2)
- C412 pad 1: VCCIO_MCU -> GND
- C413 pad 1: +1V8 -> GND
- C414 pad 1: Net-(C414-Pad1) -> VCC_1V35
- C416 pad 1: Net-(C416-Pad1) -> VCC_2V50
- C417 pad 1: VCCIO_MCU -> VCC_1V35
- C418 pad 1: +1V8 -> VCC_1V35
- C419 pad 1: Net-(C419-Pad1) -> /Cyclone V DDR3 RAM/VTT_DDR3
- C420 pad 1: Net-(C420-Pad1) -> /Cyclone V DDR3 RAM/VREF_DDR3
- C420 pad 2: Net-(C420-Pad2) -> GND
- C421 pad 1: Net-(C421-Pad1) -> VCC_1V35
- C422 pad 1: /Power Supply/VCC_SYS -> /Cyclone V DDR3 RAM/VTT_DDR3
- C423 pad 1: /Power Supply/VCC_SYS -> VCC_1V35
- C424 pad 1: Net-(C424-Pad1) -> /Cyclone V DDR3 RAM/VTT_DDR3
- C501 pad 1: VCCIO_MCU -> VCC_2V50
- C502 pad 1: +1V8 -> VCC_2V50
- C503 pad 1: VCCIO_MCU -> VCC_2V50
- C504 pad 1: VCCIO_MCU -> VCC_2V50
- C505 pad 1: Net-(C505-Pad1) -> VCC_2V50
- C506 pad 1: Net-(C506-Pad1) -> VCC_2V50
- C507 pad 1: Net-(C507-Pad1) -> GND
- C507 pad 2: GND -> VCC_2V50
- C508 pad 1: Net-(C508-Pad1) -> VCC_2V50
- C509 pad 1: Net-(C509-Pad1) -> VCC_2V50
- C510 pad 1: Net-(C510-Pad1) -> VCC_2V50
- C511 pad 1: Net-(C511-Pad1) -> VCC_2V50
- C512 pad 1: VCCIO_MCU -> VCC_2V50
- C513 pad 1: Net-(C513-Pad1) -> VCC_2V50
- C514 pad 1: Net-(C514-Pad1) -> VCC_2V50
- C601 pad 1: Net-(C601-Pad1) -> VCC_3V30
- C602 pad 1: Net-(C601-Pad1) -> VCC_3V30
- C603 pad 1: Net-(C603-Pad1) -> VCC_1V10
- C604 pad 1: Net-(C604-Pad1) -> VCC_1V10
- C605 pad 1: Net-(C605-Pad1) -> VCC_1V10
- C606 pad 1: Net-(C605-Pad1) -> VCC_1V10
- C607 pad 1: Net-(C607-Pad1) -> VCC_1V10
- C608 pad 1: VCCIO_MCU -> GND
- C608 pad 2: GND -> VCC_3V30
- C609 pad 1: Net-(C609-Pad1) -> GND
- C609 pad 2: GND -> VCC_3V30
- D501 pad 1: Net-(D501-Pad1) -> /Cyclone V FX3 FIFO/FX3_LED0
- D502 pad 1: Net-(D502-Pad1) -> /Cyclone V FX3 FIFO/FX3_LED1
- D503 pad 1: Net-(D503-Pad1) -> /Cyclone V FX3 FIFO/FX3_LED2
- JP501 pad 1: Net-(JP501-Pad1) -> VCC_2V50
- JP502 pad 1: Net-(C509-Pad1) -> Net-(JP502-Pad1)
- P601 pad 1: +1V8 -> VCC_3V30
- P601 pad 10: /Ports/PA2_N -> /Cyclone V Power/EXT_IO7
- P601 pad 2: Net-(P601-Pad2) -> GND
- P601 pad 3: +1V2 -> /Cyclone V Power/EXT_IO0
- P601 pad 4: Net-(P601-Pad4) -> /Cyclone V Power/EXT_IO1
- P601 pad 5: GND -> /Cyclone V Power/EXT_IO2
- P601 pad 6: VCCIO_MCU -> /Cyclone V Power/EXT_IO3
- P601 pad 7: /Ports/PA1_P -> /Cyclone V Power/EXT_IO4
- P601 pad 8: /Ports/PA1_N -> /Cyclone V Power/EXT_IO5
- P601 pad 9: /Ports/PA2_P -> /Cyclone V Power/EXT_IO6
- P602 pad 1: +1V8 -> VCC_3V30
- P602 pad 10: /Ports/PB2_N -> /Cyclone V Power/EXT_IO15
- P602 pad 2: Net-(P601-Pad2) -> GND
- P602 pad 3: +1V2 -> /Cyclone V Power/EXT_IO8
- P602 pad 4: Net-(C601-Pad1) -> /Cyclone V Power/EXT_IO9
- P602 pad 5: GND -> /Cyclone V Power/EXT_IO10
- P602 pad 6: VCCIO_MCU -> /Cyclone V Power/EXT_IO11
- P602 pad 7: /Ports/PB1_P -> /Cyclone V Power/EXT_IO12
- P602 pad 8: /Ports/PB1_N -> /Cyclone V Power/EXT_IO13
- P602 pad 9: /Ports/PB2_P -> /Cyclone V Power/EXT_IO14
- R201 pad 1: /SDRAM/SDRAM_D1 -> Net-(D202-Pad2)
- R201 pad 2: /SDRAM/SDRAM_D0 -> Net-(P201-Pad1)
- R202 pad 1: /SDRAM/SDRAM_D7 -> Net-(D202-Pad1)
- R202 pad 2: /SDRAM/SDRAM_D6 -> Net-(R202-Pad2)
- R203 pad 1: Net-(R203-Pad1) -> Net-(R202-Pad2)
- R203 pad 2: Net-(R203-Pad2) -> GND
- R204 pad 1: Net-(R204-Pad1) -> /FX3 USB & Power Supply/VCC_IN
- R204 pad 2: Net-(R204-Pad2) -> Net-(C216-Pad1)
- R205 pad 1: /SDRAM/SDRAM_D17 -> Net-(D205-Pad1)
- R205 pad 2: /SDRAM/SDRAM_D16 -> GND
- R206 pad 1: /SDRAM/SDRAM_D23 -> Net-(R206-Pad1)
- R206 pad 2: /SDRAM/SDRAM_D22 -> GND
- R207 pad 2: Net-(R207-Pad2) -> GND
- R208 pad 1: Net-(R208-Pad1) -> Net-(Q202-Pad1)
- R208 pad 2: Net-(R208-Pad2) -> ~RESET~
- R301 pad 1: GND -> /Cyclone V User IO/VREF_B4
- R301 pad 2: VCCIO_MCU -> /Cyclone V User IO/VCCIO_IO_A
- R302 pad 1: VCCIO_MCU -> GND
- R302 pad 2: GND -> /Cyclone V User IO/VREF_B4
- R303 pad 1: Net-(D304-Pad2) -> /Cyclone V User IO/VREF_B5A
- R303 pad 2: Net-(D303-Pad2) -> /Cyclone V User IO/VCCIO_IO_B
- R401 pad 1: Net-(D402-Pad2) -> /Cyclone V DDR3 RAM/FPGA_DDR3_CKE
- R401 pad 2: Net-(P401-Pad1) -> GND
- R402 pad 1: MCU_TWD0 -> Net-(R402-Pad1)
- R402 pad 2: MCU_TWCK0 -> GND
- R403 pad 1: Net-(D404-Pad1) -> /Cyclone V DDR3 RAM/FPGA_DDR3_ODT
- R403 pad 2: Net-(R403-Pad2) -> /Cyclone V DDR3 RAM/~FPGA_DDR3_WE~
- R404 pad 1: Net-(C414-Pad1) -> /Cyclone V DDR3 RAM/FPGA_DDR3_A6
- R404 pad 2: Net-(C419-Pad1) -> /Cyclone V DDR3 RAM/FPGA_DDR3_A8
- R405 pad 1: VCCBU_MCU -> /Cyclone V DDR3 RAM/FPGA_DDR3_A10
- R405 pad 2: Net-(Q402-Pad1) -> /Cyclone V DDR3 RAM/FPGA_DDR3_A15
- R405 pad 3: /Power Supply/~MCU_SHDN~ -> /Cyclone V DDR3 RAM/FPGA_DDR3_BA1
- R405 pad 4: Net-(Q402-Pad3) -> /Cyclone V DDR3 RAM/FPGA_DDR3_A4
- R405 pad 5: Net-(C427-Pad1) -> /Cyclone V DDR3 RAM/VTT_DDR3
- R405 pad 6: VCCBU_MCU -> /Cyclone V DDR3 RAM/VTT_DDR3
- R405 pad 7: VCCBU_MCU -> /Cyclone V DDR3 RAM/VTT_DDR3
- R405 pad 8: /Power Supply/MCU_FWUP -> /Cyclone V DDR3 RAM/VTT_DDR3
- R406 pad 1: GND -> (no net)
- R406 pad 2: Net-(D405-Pad1) -> /Cyclone V DDR3 RAM/FPGA_DDR3_CK_P
- R407 pad 1: Net-(C424-Pad1) -> (no net)
- R407 pad 2: Net-(C427-Pad1) -> /Cyclone V DDR3 RAM/FPGA_CLK10_N
- R408 pad 1: VCCIO_MCU -> /Cyclone V DDR3 RAM/FPGA_DDR3_A9
- R408 pad 2: Net-(R408-Pad2) -> /Cyclone V DDR3 RAM/FPGA_DDR3_A13
- R409 pad 1: Net-(R408-Pad2) -> /Cyclone V DDR3 RAM/FPGA_DDR3_A3
- R409 pad 2: GND -> /Cyclone V DDR3 RAM/FPGA_DDR3_BA2
- R410 pad 1: VCCIO_MCU -> /Cyclone V DDR3 RAM/FPGA_DDR3_A1
- R410 pad 2: Net-(R410-Pad2) -> /Cyclone V DDR3 RAM/FPGA_DDR3_A12
- R411 pad 1: Net-(R410-Pad2) -> VCC_1V35
- R411 pad 2: GND -> Net-(C415-Pad1)
- R412 pad 1: Net-(R412-Pad1) -> Net-(C415-Pad1)
- R413 pad 1: Net-(R413-Pad1) -> /Cyclone V DDR3 RAM/VTT_DDR3_PGOOD
- R413 pad 2: GND -> VCC_1V35
- R414 pad 1: Net-(R412-Pad1) -> Net-(R414-Pad1)
- R414 pad 2: +1V8 -> GND
- R501 pad 1: Net-(R501-Pad1) -> VCC_2V50
- R502 pad 1: Net-(D504-Pad2) -> Net-(JP501-Pad2)
- R502 pad 2: Net-(D503-Pad2) -> Net-(R502-Pad2)
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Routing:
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- added copper zone on B.Cu, net GND
- added copper zone on In3.Cu, net GND
- added copper zone on In1.Cu, net VCC_1V35
- removed copper zone on F.Cu, net +1V2
- removed copper zone on F.Cu, net +1V8
- removed copper zone on F.Cu, net GND
- removed copper zone on In1.Cu, net GND
- removed copper zone on F.Cu, net Net-(C424-Pad1)
- removed copper zone on F.Cu, net Net-(L404-Pad1)
- removed copper zone on F.Cu, net Net-(L405-Pad1)
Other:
- board outline removed
- copper layers 4 -> 6
- net class DDR3_100Ohm added: clearance 0.102, trace_width 0.102, via_dia 0.46, via_drill 0.254
- net class DDR3_50Ohm added: clearance 0.102, trace_width 0.102, via_dia 0.46, via_drill 0.254
- net class Default: clearance 0.15 -> 0.102; trace_width 0.3 -> 0.102; via_dia 0.6 -> 0.46; via_drill 0.3 -> 0.254
- net class FPGA removed
- net class Impedance 100 Ohm removed
- net class Power removed
- rule trace_clearance: 0.15 -> 0.102
- rule trace_min: 0.125 -> 0.102
- rule via_min_drill: 0.1 -> 0.254
- rule via_min_size: 0.45 -> 0.458
